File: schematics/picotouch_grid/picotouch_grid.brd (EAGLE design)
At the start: 157.5 x 105.4 mm, 140 parts, among them J1 AUDIO-JACK-TRRS, J2 STEMMA_I2C_QT, K1 TOUCHKEYH, K10 TOUCHKEYH, K11 TOUCHKEYH, K12 TOUCHKEYH, K13 TOUCHKEYH, K14 TOUCHKEYH, K15 TOUCHKEYH, K16 TOUCHKEYH, K17 TOUCHKEYH, K18 TOUCHKEYH, K19 TOUCHKEYH, K2 TOUCHKEYH, K20 TOUCHKEYH, K21 TOUCHKEYH, K22 TOUCHKEYH, K23 TOUCHKEYH, K24 TOUCHKEYH, K25 TOUCHKEYH, K26 TOUCHKEYH, K27 TOUCHKEYH, K28 TOUCHKEYH, K29 TOUCHKEYH, K3 TOUCHKEYH, K30 TOUCHKEYH, K31 TOUCHKEYH, K32 TOUCHKEYH, K33 TOUCHKEYH, K34 TOUCHKEYH, K35 TOUCHKEYH, K36 TOUCHKEYH, K37 TOUCHKEYH, K38 TOUCHKEYH, K39 TOUCHKEYH, K4 TOUCHKEYH, K40 TOUCHKEYH, K5 TOUCHKEYH, K6 TOUCHKEYH, K7 TOUCHKEYH, K8 TOUCHKEYH, K9 TOUCHKEYH, U1 RASPBERRY_PICOSMD

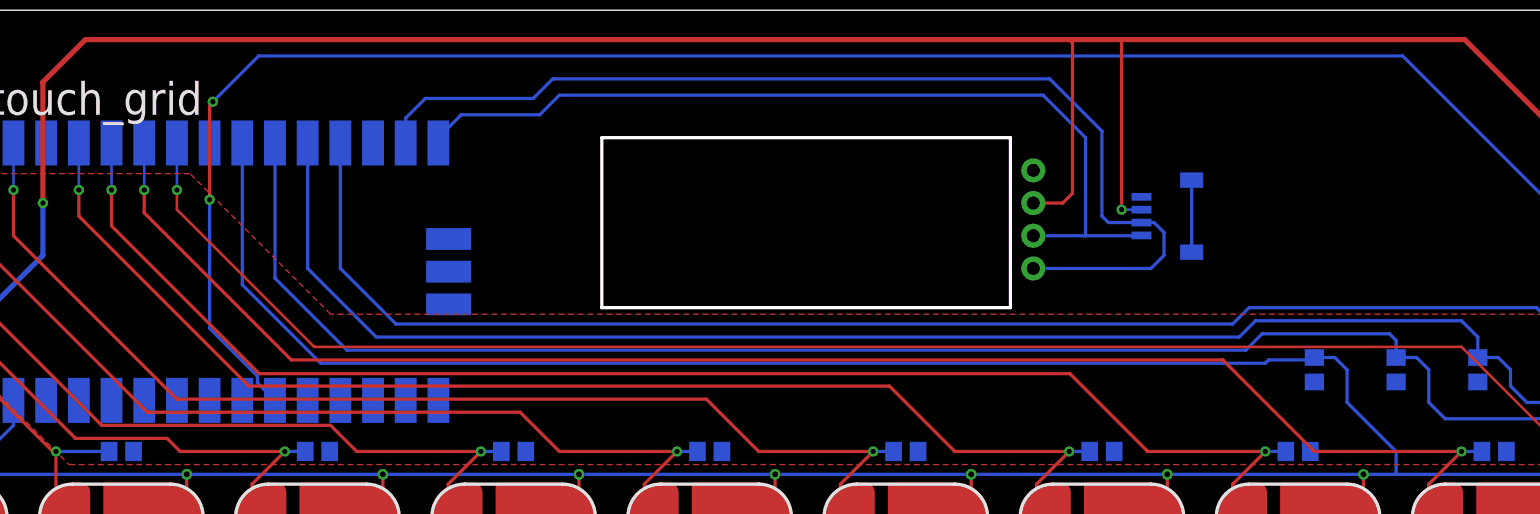
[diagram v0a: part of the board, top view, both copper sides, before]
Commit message: added gpio pins 16,17,18,19 as smd touchpads for hacking
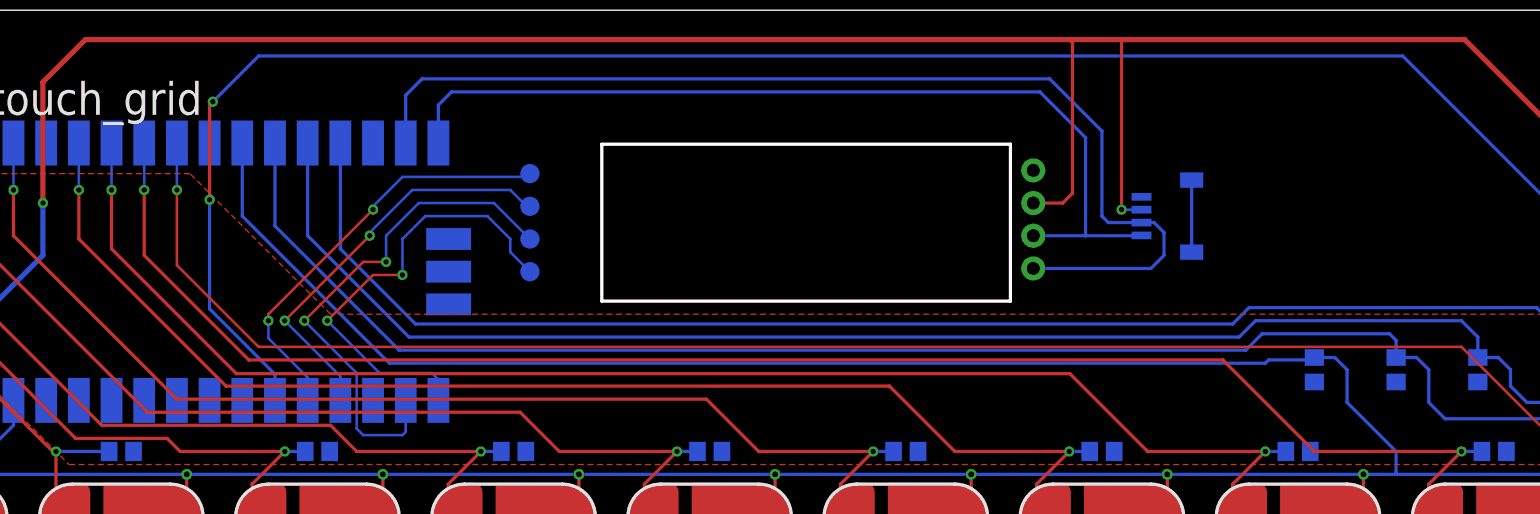
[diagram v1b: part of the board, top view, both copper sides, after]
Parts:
- added 16, 17, 18, 19: TPTP15R, testpad:TP15R
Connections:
- new net N$39: 16.TP, U1.P$21
- new net N$40: 17.TP, U1.P$22
- new net N$41: 18.TP, U1.P$24
- new net N$42: 19.TP, U1.P$25
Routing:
- net N$40: track 0.00 -> 40.3 mm, vias 0 -> 2
- net N$39: track 0.00 -> 35.3 mm, vias 0 -> 2
- net N$42: track 0.00 -> 33.0 mm, vias 0 -> 2
- net N$41: track 0.00 -> 31.9 mm, vias 0 -> 2
- net ROW1: track 267.2 -> 264.0 mm
- net COL10: track 194.2 -> 196.7 mm
- net ROW2: track 318.9 -> 316.5 mm
- net COL9: track 181.6 -> 183.5 mm
- net SCL: track 69.5 -> 71.2 mm
- net ROW3: track 333.8 -> 332.3 mm
- net SDA: track 83.3 -> 84.3 mm
- net COL8: track 169.5 -> 170.5 mm
- net COL7: track 156.4 -> 157.4 mm
- net ROW4: track 349.6 -> 348.7 mm
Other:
- outline, holes or cut-outs redrawn
- board text added: "https://github.com/todbot/picotouch 16 Jan 2023 - @todbot"
- board text removed: "https://github.com/todbot/picotouch 30 Jan 2023 - @todbot"

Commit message: added test points
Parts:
- added 3V3, 3VM, GND, M, NEOPIXEL: TPTP15R, testpad:TP15R
- moved R15 2.55 mm to (138.9, 94.0)
- moved R16 2.55 mm to (139.2, 87.4)
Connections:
- net +3V3: now also 3V3.TP
- net GND: now also GND.TP
- net N$38: now also 3VM.TP
- net N$8: now also M.TP
- net NEOPIXEL: now also NEOPIXEL.TP
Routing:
- net N$8: track 9.14 -> 13.4 mm
- net NEOPIXEL: track 21.7 -> 25.3 mm
- net N$38: track 11.4 -> 14.1 mm
- net MIDI_OUT: track 141.1 -> 138.6 mm
- net +3V3: track 989.4 -> 987.0 mm
